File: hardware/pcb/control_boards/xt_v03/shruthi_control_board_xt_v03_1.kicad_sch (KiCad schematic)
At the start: 29 parts, among them IC1 24LC512, IC10 ATMEGA644p, J1 CV, J2 POWER, J3 M03PTH, J4 POWER, Q1 20MHz, U1 AVRISP, X1 MIDI, X2 MIDI

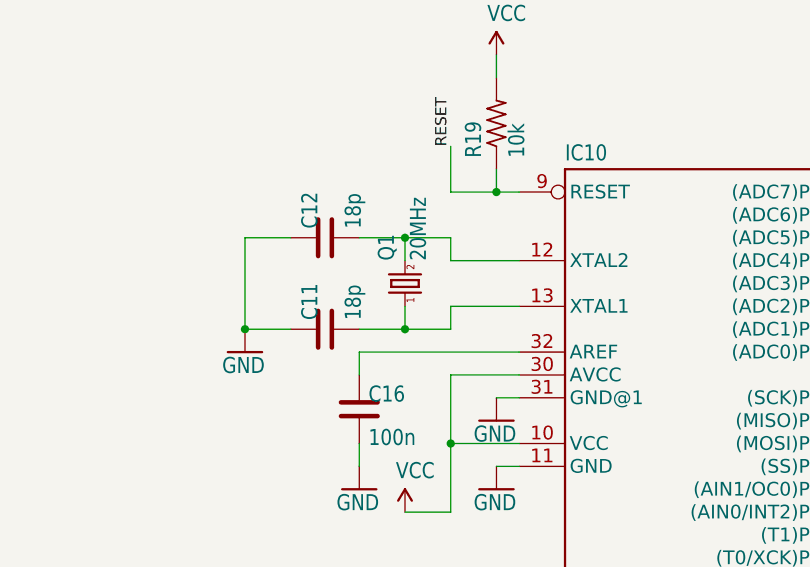
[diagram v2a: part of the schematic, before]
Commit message: update crystal to use kicad symbols
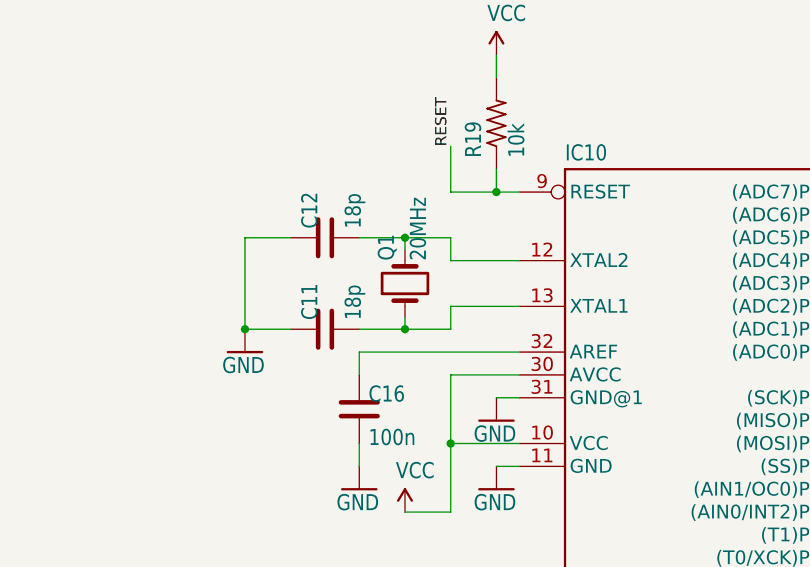
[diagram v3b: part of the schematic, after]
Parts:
- Q1: symbol shruthi_control_board_xt_v03-eagle-import:CRYSTALHC49U-V -> Device:Crystal
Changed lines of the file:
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@@
 	)
 	(junction
+		(at 142.24 116.84)
+		(diameter 0)
+		(color 0 0 0 0)
+	)
+	(junction
 		(at 248.92 162.56)
 		(diameter 0)
@@
 	)
 	(junction
-		(at 332.74 111.76)
+		(at 142.24 106.68)
 		(diameter 0)
 		(color 0 0 0 0)
 	)
 	(junction
-		(at 142.24 106.68)
+		(at 332.74 111.76)
 		(diameter 0)
 		(color 0 0 0 0)
@@
 	)
 	(junction
-		(at 142.24 116.84)
-		(diameter 0)
-		(color 0 0 0 0)
-	)
-	(junction
 		(at 210.82 248.92)
 		(diameter 0)
@@
 	(wire
 		(pts
+			(xy 142.24 116.84) (xy 147.32 116.84)
+		)
+		(stroke
+			(width 0.1524)
+			(type solid)
+		)
+	)
+	(wire
+		(pts
 			(xy 147.32 116.84) (xy 147.32 114.3)
 		)
@@
 	(wire
 		(pts
-			(xy 142.24 106.68) (xy 147.32 106.68)
+			(xy 137.16 106.68) (xy 142.24 106.68)
 		)
 		(stroke
@@
 	(wire
 		(pts
-			(xy 142.24 116.84) (xy 142.24 114.3)
-		)
-		(stroke
-			(width 0.1524)
-			(type solid)
-		)
-	)
-	(wire
-		(pts
 			(xy 238.76 111.76) (xy 236.22 111.76)
 		)
@@
 	(wire
 		(pts
+			(xy 142.24 115.57) (xy 142.24 116.84)
+		)
+		(stroke
+			(width 0)
+			(type default)
+		)
+	)
+	(wire
+		(pts
 			(xy 152.4 101.6) (xy 152.4 99.06)
 		)
@@
 	(wire
 		(pts
+			(xy 142.24 106.68) (xy 142.24 107.95)
+		)
+		(stroke
+			(width 0)
+			(type default)
+		)
+	)
+	(wire
+		(pts
 			(xy 309.88 111.76) (xy 320.04 111.76)
 		)
@@
 	(wire
 		(pts
-			(xy 137.16 106.68) (xy 142.24 106.68)
-		)
-		(stroke
-			(width 0.1524)
-			(type solid)
-		)
-	)
-	(wire
-		(pts
 			(xy 195.58 124.46) (xy 198.12 124.46)
 		)
@@
 	(wire
 		(pts
-			(xy 142.24 116.84) (xy 147.32 116.84)
-		)
-		(stroke
-			(width 0.1524)
-			(type solid)
-		)
-	)
-	(wire
-		(pts
 			(xy 261.62 111.76) (xy 261.62 114.3)
 		)
@@
 	(wire
 		(pts
-			(xy 142.24 106.68) (xy 142.24 109.22)
-		)
-		(stroke
-			(width 0.1524)
-			(type solid)
-		)
-	)
-	(wire
-		(pts
 			(xy 147.32 101.6) (xy 152.4 101.6)
 		)
@@
 	(wire
 		(pts
+			(xy 142.24 106.68) (xy 147.32 106.68)
+		)
+		(stroke
+			(width 0.1524)
+			(type solid)
+		)
+	)
+	(wire
+		(pts
 			(xy 195.58 137.16) (xy 198.12 137.16)
 		)
@@
 	)
 	(symbol
-		(lib_id "shruthi_control_board_xt_v03-eagle-import:CRYSTALHC49U-V")
+		(lib_id "Device:Crystal")
 		(at 142.24 111.76 90)
 		(unit 1)
@@
 			)
 		)
-		(property "Datasheet" ""
+		(property "Datasheet" "~"
 			(at 142.24 111.76 0)
 			(effects
@@
 			)
 		)
-		(property "Description" ""
+		(property "Description" "Two pin crystal"
 			(at 142.24 111.76 0)
 			(effects
